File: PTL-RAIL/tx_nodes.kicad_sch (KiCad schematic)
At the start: 0 parts

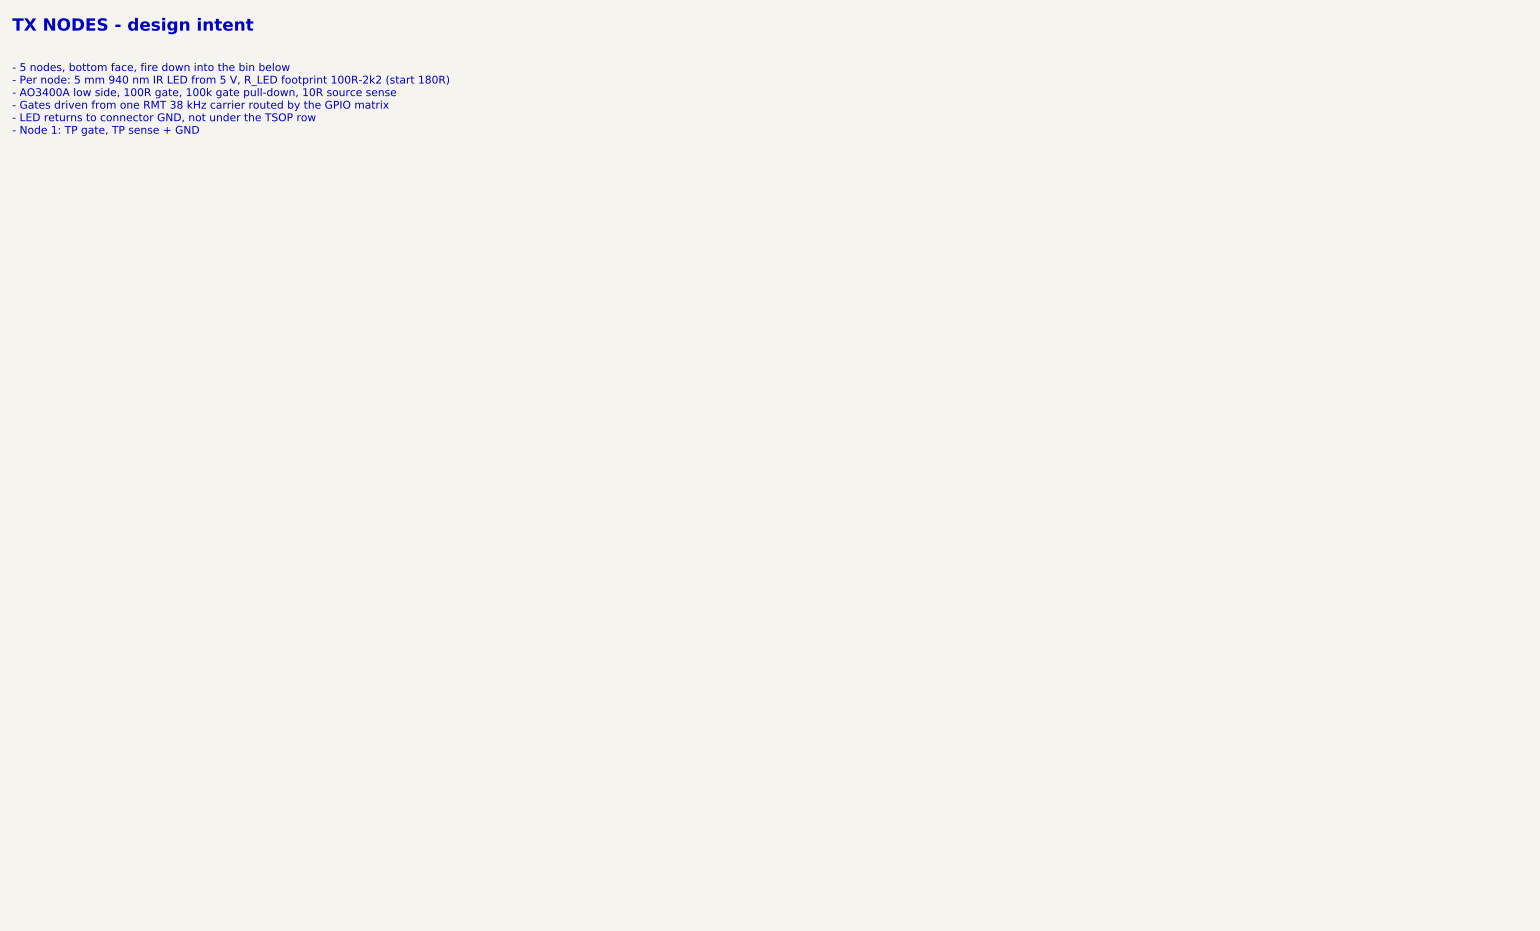
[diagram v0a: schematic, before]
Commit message: PTL-RAIL: LED row on top edge, TSOP row on bottom edge, node parts aligned at 84 mm pitch; J3/J4 10-way and J5/J6 4-way screw terminals
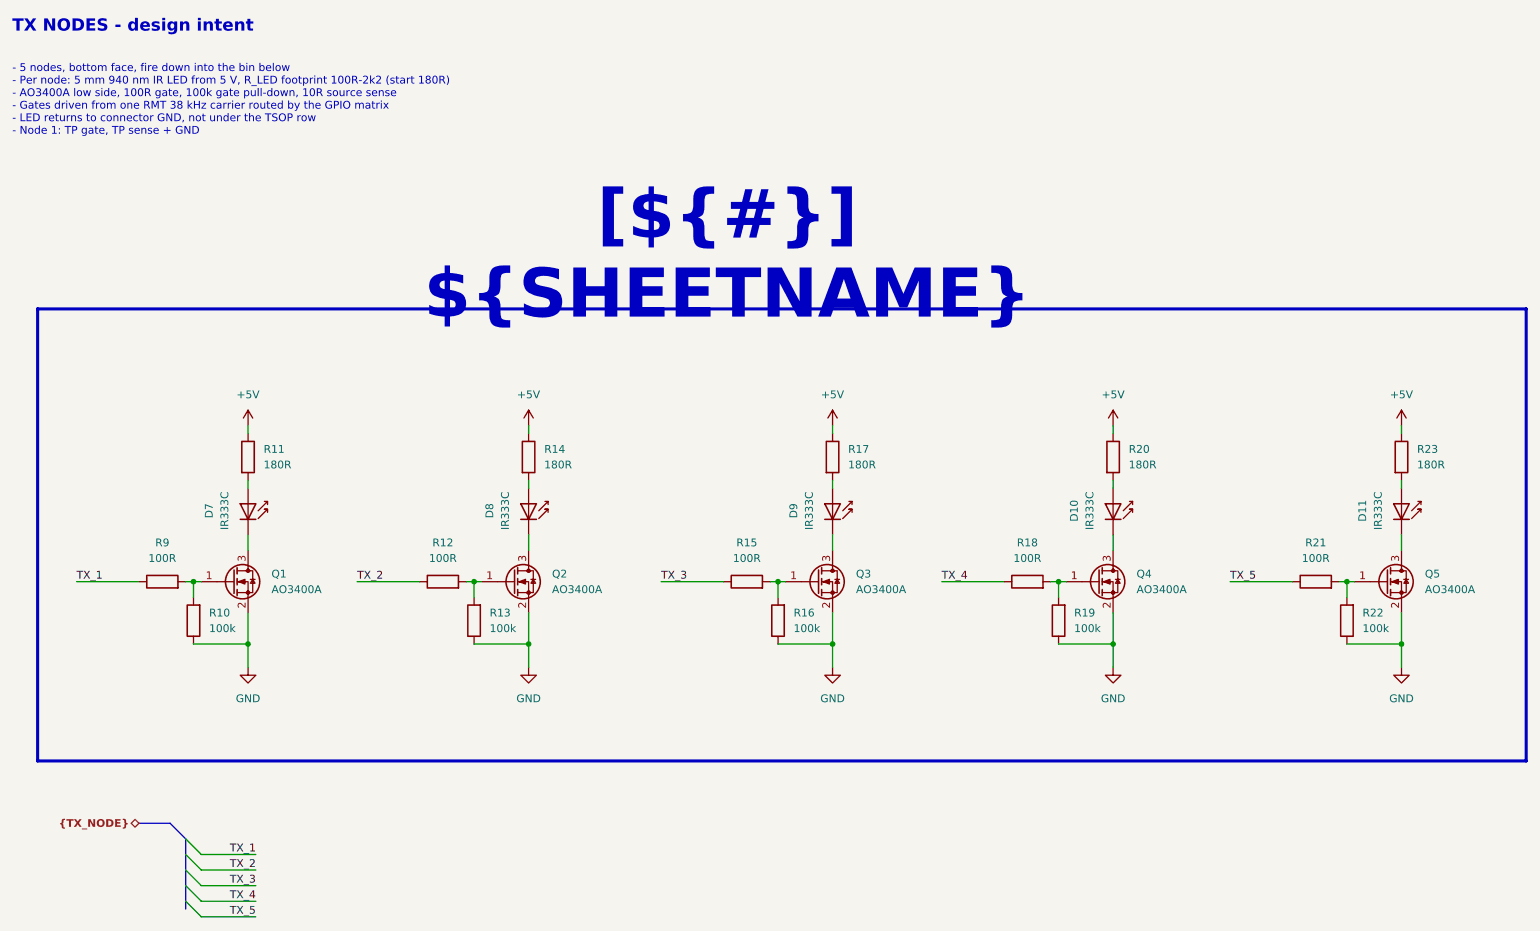
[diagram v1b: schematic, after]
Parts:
- added D10, D11, D7, D8, D9: IR333C, LED_THT:LED_D5.0mm_Horizontal_O1.27mm_Z3.0mm_IRGrey, symbol LED:CQY99
- added Q1, Q2, Q3, Q4, Q5: AO3400A, Package_TO_SOT_SMD:SOT-23, symbol Transistor_FET:AO3400A
- added R10, R13, R16, R19, R22: 100k, Resistor_SMD:R_0805_2012Metric, symbol Device:R
- added R11, R14, R17, R20, R23: 180R, Resistor_SMD:R_0805_2012Metric, symbol Device:R
- added R12, R15, R18, R21, R9: 100R, Resistor_SMD:R_0805_2012Metric, symbol Device:R
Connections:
- new net: Q1.1 (G), R10.2, R9.2
- new net: Q3.1 (G), R15.2, R16.2
- new net: D8.2 (A), R14.2
- new net: D7.1 (K), Q1.3 (D)
- new net: Q2.1 (G), R12.2, R13.2
- new net: D8.1 (K), Q2.3 (D)
- new net: Q5.1 (G), R21.2, R22.2
- new net: D11.1 (K), Q5.3 (D)
- new net: D10.1 (K), Q4.3 (D)
- new net: D10.2 (A), R20.2
- new net: D9.2 (A), R17.2
- new net: D9.1 (K), Q3.3 (D)
- new net: Q4.1 (G), R18.2, R19.2
- new net: D7.2 (A), R11.2
- new net: D11.2 (A), R23.2
- new net +5V: R11.1, R14.1, R17.1, R20.1, R23.1
- new net GND: Q1.2 (S), Q2.2 (S), Q3.2 (S), Q4.2 (S), Q5.2 (S), R10.1, R13.1, R16.1, R19.1, R22.1
- new net TX_1: R9.1
- new net TX_2: R12.1
- new net TX_3: R15.1
- new net TX_4: R18.1
- new net TX_5: R21.1
